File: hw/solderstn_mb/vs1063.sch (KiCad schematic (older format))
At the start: 0 parts

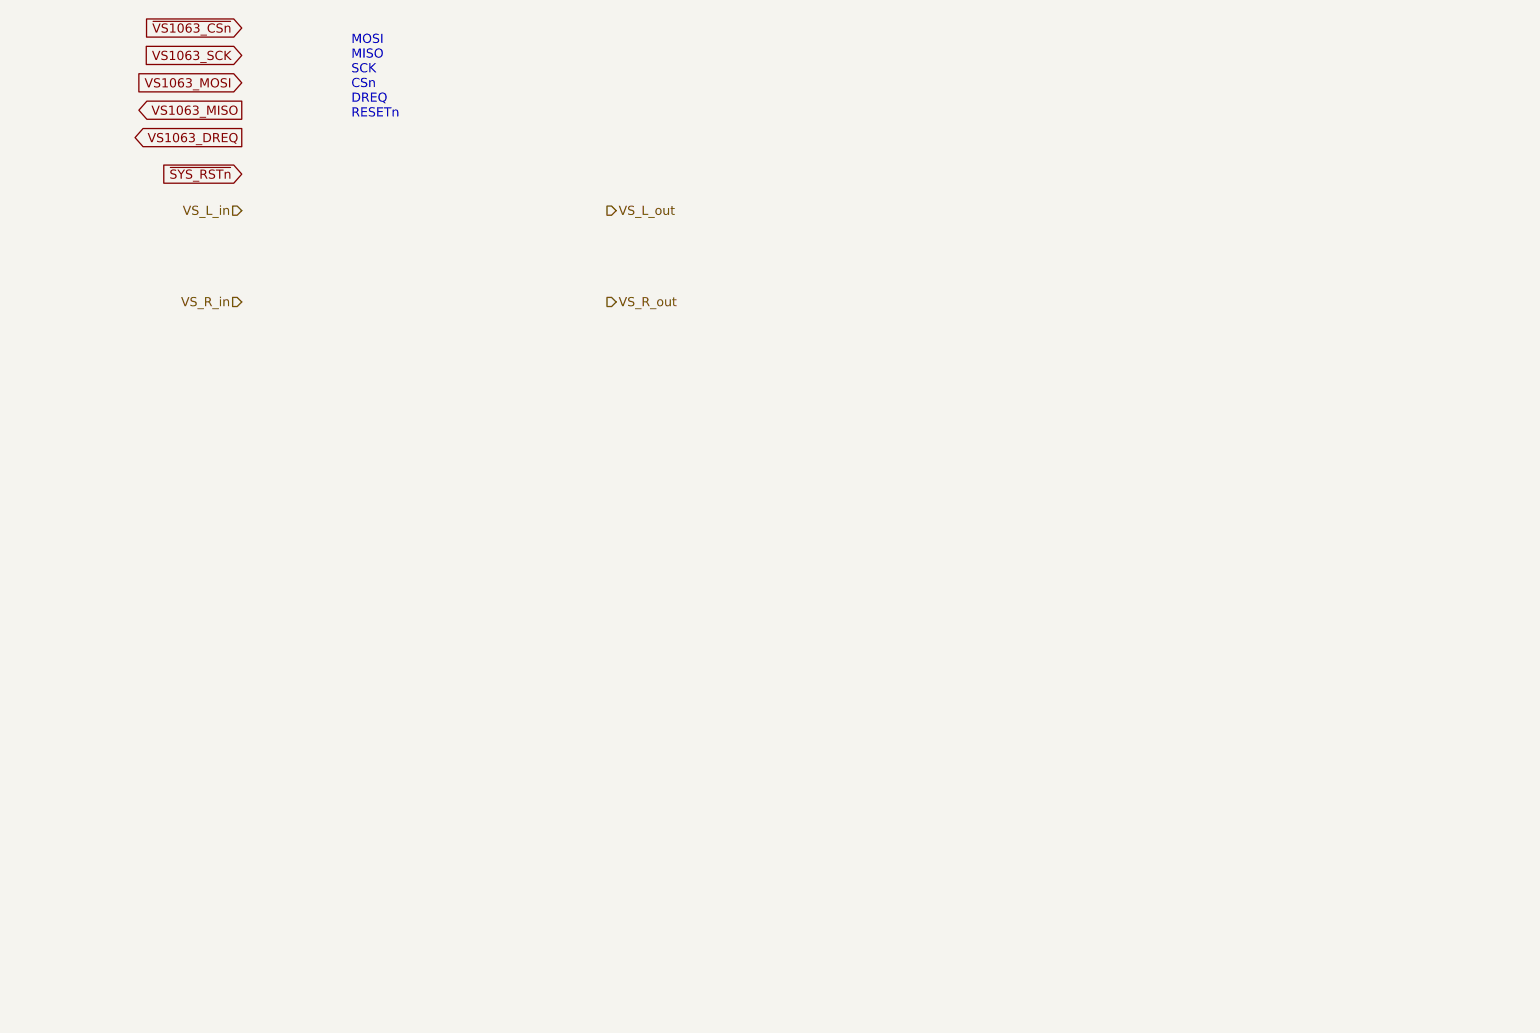
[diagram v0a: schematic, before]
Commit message: MB - Sch design: VS1063 in new audio path; Added: some new ESD, some fixups; Changes: some footprints, fixes
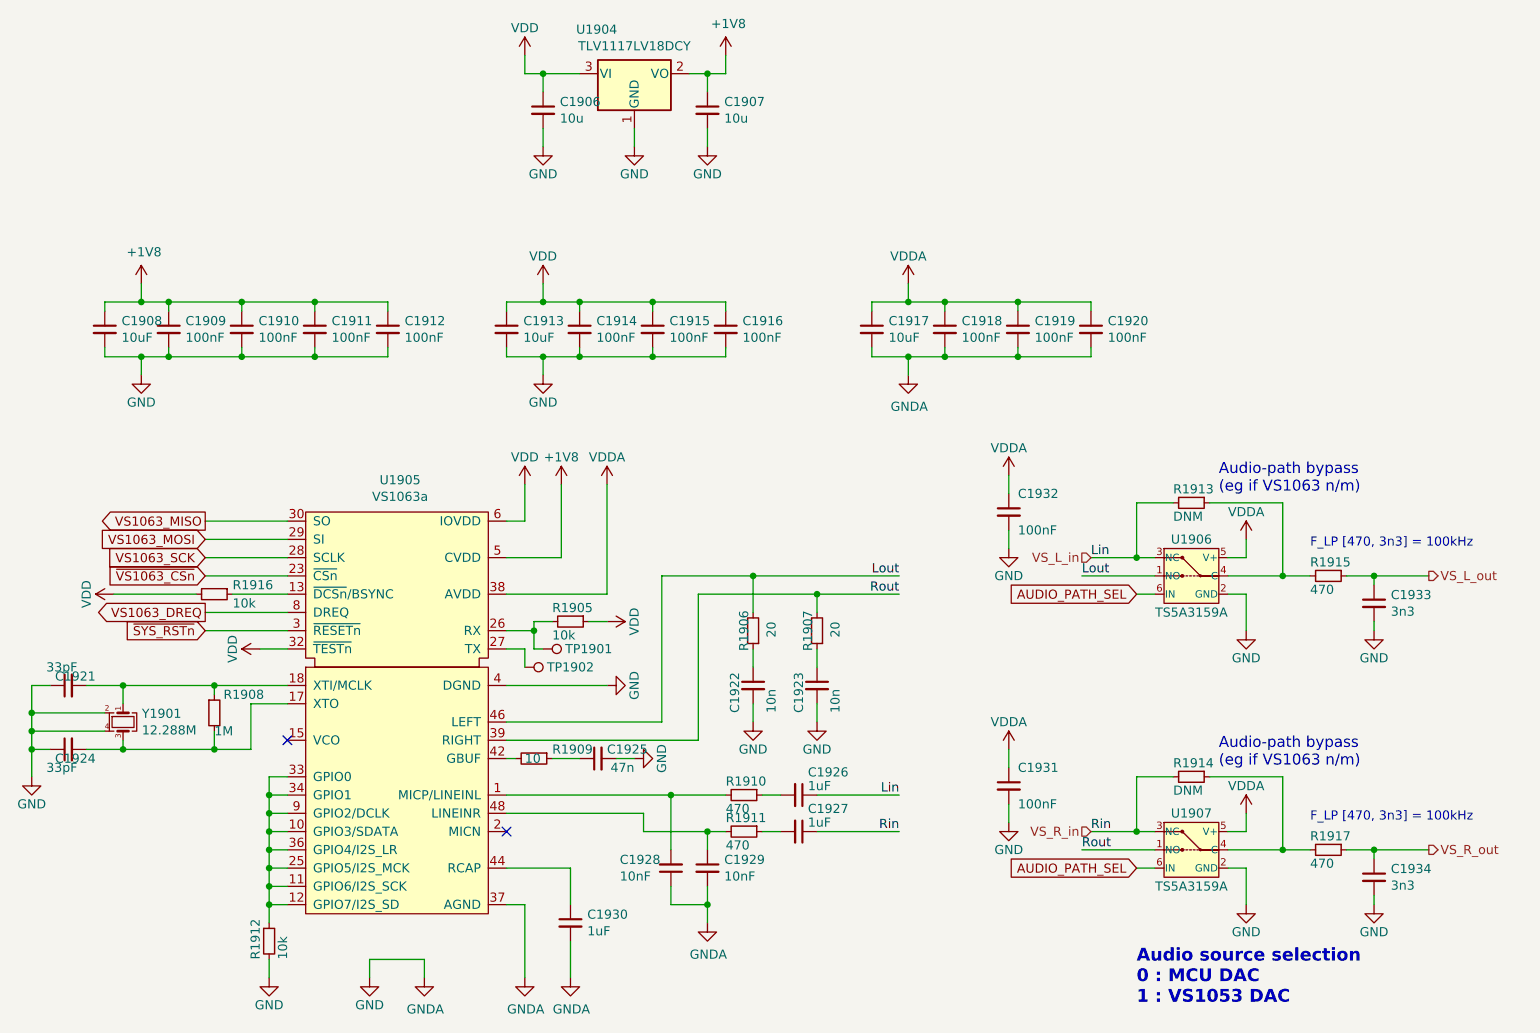
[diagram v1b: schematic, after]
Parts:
- added C1906, C1907: 10u, Capacitor_SMD:C_0603_1608Metric, symbol Device:C_Small
- added C1908, C1913, C1917: 10uF, Capacitor_SMD:C_0603_1608Metric, symbol Device:C_Small
- added C1909, C1910, C1911, C1912, C1914, C1915, C1916, C1918, C1919, C1920, C1931, C1932: 100nF, Capacitor_SMD:C_0402_1005Metric, symbol Device:C_Small
- added C1921, C1924: 33pF, Capacitor_SMD:C_0402_1005Metric, symbol Device:C_Small
- added C1922, C1923: 10n, Capacitor_SMD:C_0402_1005Metric, symbol Device:C_Small
- added C1925: 47n, Capacitor_SMD:C_0402_1005Metric, symbol Device:C_Small
- added C1926, C1927, C1930: 1uF, Capacitor_SMD:C_0603_1608Metric, symbol Device:C_Small
- added C1928, C1929: 10nF, Capacitor_SMD:C_0402_1005Metric, symbol Device:C_Small
- added C1933, C1934: 3n3, Capacitor_SMD:C_0402_1005Metric, symbol Device:C_Small
- added R1905, R1912, R1916: 10k, Resistor_SMD:R_0402_1005Metric, symbol customlib_mj:R_Small
- added R1906, R1907: 20, Resistor_SMD:R_0402_1005Metric, symbol customlib_mj:R_Small
- added R1908: 1M, Resistor_SMD:R_0402_1005Metric, symbol customlib_mj:R_Small
- added R1909: 10, Resistor_SMD:R_0402_1005Metric, symbol customlib_mj:R_Small
- added R1910, R1911, R1915, R1917: 470, Resistor_SMD:R_0402_1005Metric, symbol customlib_mj:R_Small
- added R1913, R1914: DNM, Resistor_SMD:R_0603_1608Metric, symbol customlib_mj:R_Small
- added TP1901, TP1902: TP, customlib_mj_fp:TP_SMD_1.2c, symbol customlib_mj:TP
- added U1904: TLV1117LV18DCY, Package_TO_SOT_SMD:SOT-223-3_TabPin2, symbol customlib_mj:TLV1117LV30DCY
- added U1905: VS1063a, Package_QFP:LQFP-48_7x7mm_P0.5mm, symbol customlib_mj:VS1063a
- added U1906, U1907: TS5A3159A, Package_TO_SOT_SMD:SOT-23-6, symbol customlib_mj:TS5A3159A
- added Y1901: 12.288M, Crystal:Crystal_SMD_SeikoEpson_TSX3225-4Pin_3.2x2.5mm_HandSoldering, symbol customlib_mj:Crystal_ECS­122.8­18­33­JGN­TR
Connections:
- net VS1063_DREQ: now also U1905.8 (DREQ)
- net VS1063_MISO: now also U1905.30 (SO)
- net VS1063_MOSI: now also U1905.29 (SI)
- net VS1063_SCK: now also U1905.28 (SCLK)
- net VS_L_in: now also C1926.1, R1913.2, U1906.3 (NC)
- net VS_L_out: now also C1933.1, R1915.1
- net VS_R_in: now also C1927.1, R1914.2, U1907.3 (NC)
- net VS_R_out: now also C1934.1, R1917.1
- net ~SYS_RSTn~: now also U1905.3 (~RESETn~)
- net ~VS1063_CSn~: now also U1905.23 (~CSn~)
- new net: C1928.2, R1910.2, U1905.1 (MICP/LINEINL)
- new net: R1912.1, U1905.10 (GPIO3/SDATA), U1905.11 (GPIO6/I2S_SCK), U1905.12 (GPIO7/I2S_SD), U1905.25 (GPIO5/I2S_MCK), U1905.33 (GPIO0), U1905.34 (GPIO1), U1905.36 (GPIO4/I2S_LR), U1905.9 (GPIO2/DCLK)
- new net: R1916.1, U1905.13 (~DCSn~/BSYNC)
- new net: C1924.2, R1908.2, U1905.17 (XTO), Y1901.3
- new net: C1921.2, R1908.1, U1905.18 (XTI/MCLK), Y1901.1
- new net: R1905.2, TP1901.1, U1905.26 (RX)
- new net: TP1902.1, U1905.27 (TX)
- new net: R1909.2, U1905.42 (GBUF)
- new net: C1930.1, U1905.44 (RCAP)
- new net: C1929.1, R1911.2, U1905.48 (LINEINR)
- new net: C1926.2, R1910.1
- new net: C1927.2, R1911.1
- new net: C1925.1, R1909.1
- new net: C1923.1, R1907.1
- new net: C1922.1, R1906.1
- new net: R1913.1, R1915.2, U1906.4 (C)
- new net: R1914.1, R1917.2, U1907.4 (C)
- new net +1V8: C1907.1, C1908.1, C1909.1, C1910.1, C1911.1, C1912.1, U1904.2 (VO), U1905.24 (CVDD), U1905.31 (CVDD), U1905.5 (CVDD), U1905.7 (CVDD)
- new net AGND: C1906.2, C1907.2, C1908.2, C1909.2, C1910.2, C1911.2, C1912.2, C1913.2, C1914.2, C1915.2, C1916.2, C1917.2, C1918.2, C1919.2, C1920.2, C1921.1, C1922.2, C1923.2, C1924.1, C1925.2, C1928.1, C1929.2, C1930.2, C1931.2, C1932.2, C1933.2, C1934.2, R1912.2, U1904.1 (GND), U1905.16 (DGND), U1905.20 (DGND), U1905.21 (DGND), U1905.22 (DGND), U1905.35 (DGND), U1905.37 (AGND), U1905.4 (DGND), U1905.40 (AGND), U1905.41 (AGND), U1905.47 (AGND), U1906.2 (GND), U1907.2 (GND), Y1901.2, Y1901.4
- new net AUDIO_PATH_SEL: U1906.6 (IN), U1907.6 (IN)
- new net AVDD: C1917.1, C1918.1, C1919.1, C1920.1, C1931.1, C1932.1, U1905.38 (AVDD), U1905.43 (AVDD), U1905.45 (AVDD), U1906.5 (V+), U1907.5 (V+)
- new net IOVDD: C1906.1, C1913.1, C1914.1, C1915.1, C1916.1, R1905.1, R1916.2, U1904.3 (VI), U1905.14 (IOVDD), U1905.19 (IOVDD), U1905.32 (~TESTn~), U1905.6 (IOVDD)
- new net Lout: R1906.2, U1905.46 (LEFT), U1906.1 (NO)
- new net Rout: R1907.2, U1905.39 (RIGHT), U1907.1 (NO)
- no-connect marks 0 -> 2
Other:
- note added: "Audio source selection\n0 : MCU DAC\n1 : VS1053 DAC"
- note added: "Audio-path bypass\n(eg if VS1063 n/m)"
- note added: "F_LP [470, 3n3] = 100kHz"
- note removed: "MOSI\nMISO\nSCK\nCSn\nDREQ\nRESETn"

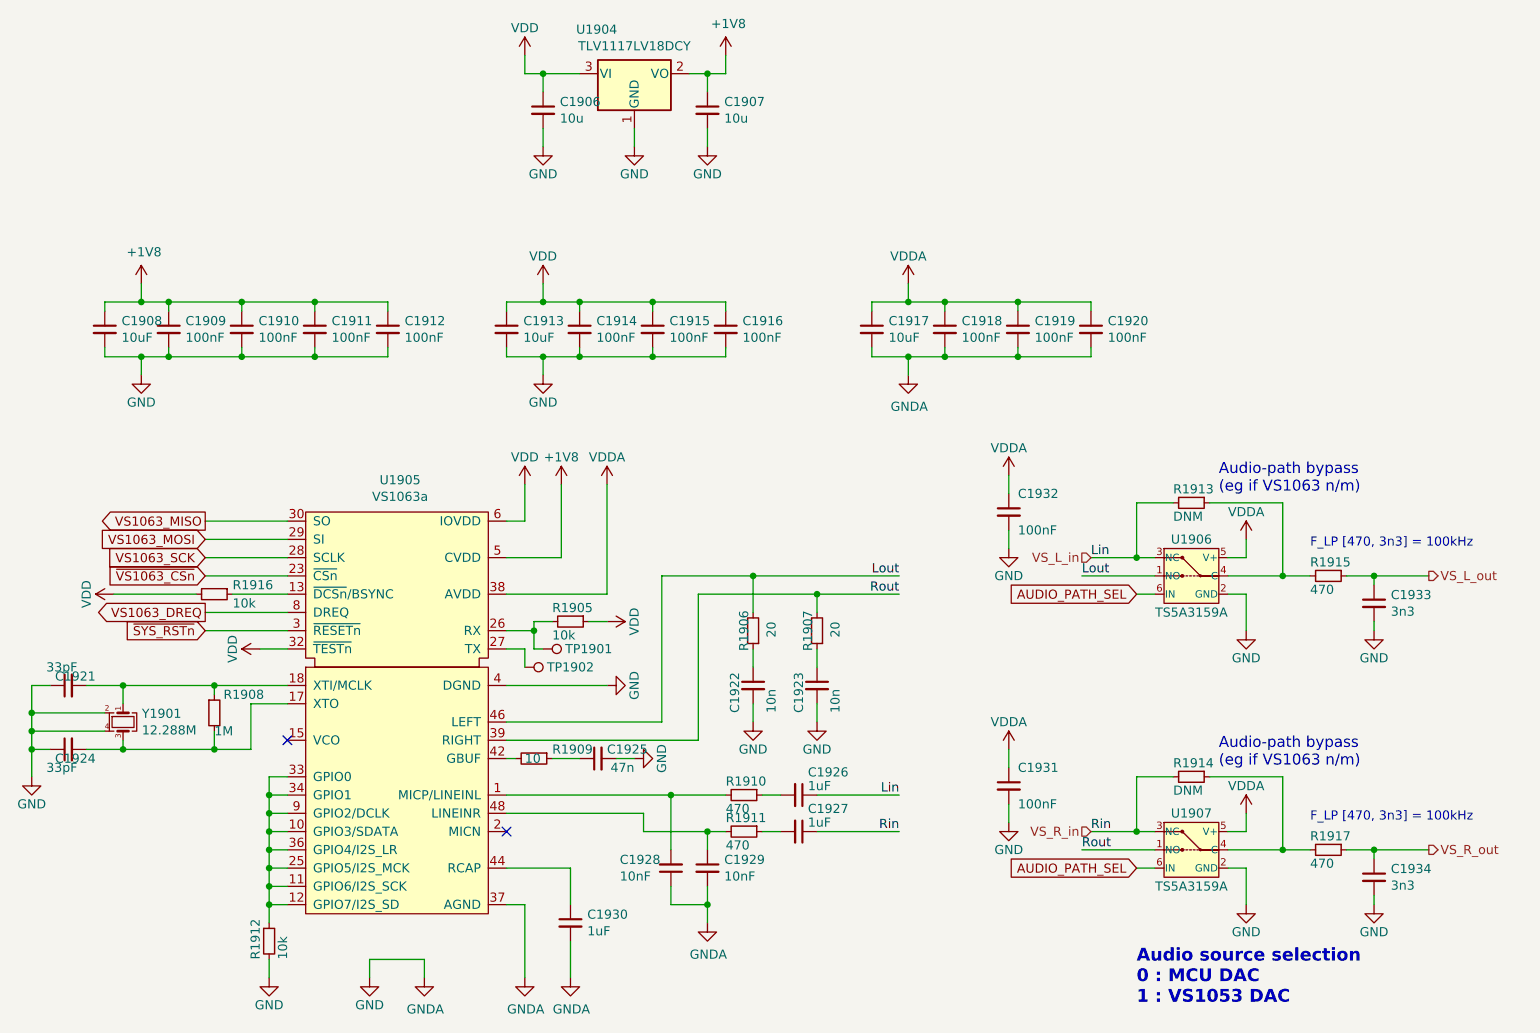
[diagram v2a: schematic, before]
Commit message: Reannotate entire schematic; add temp.extra SMA-conn to eval alternative FMI placement
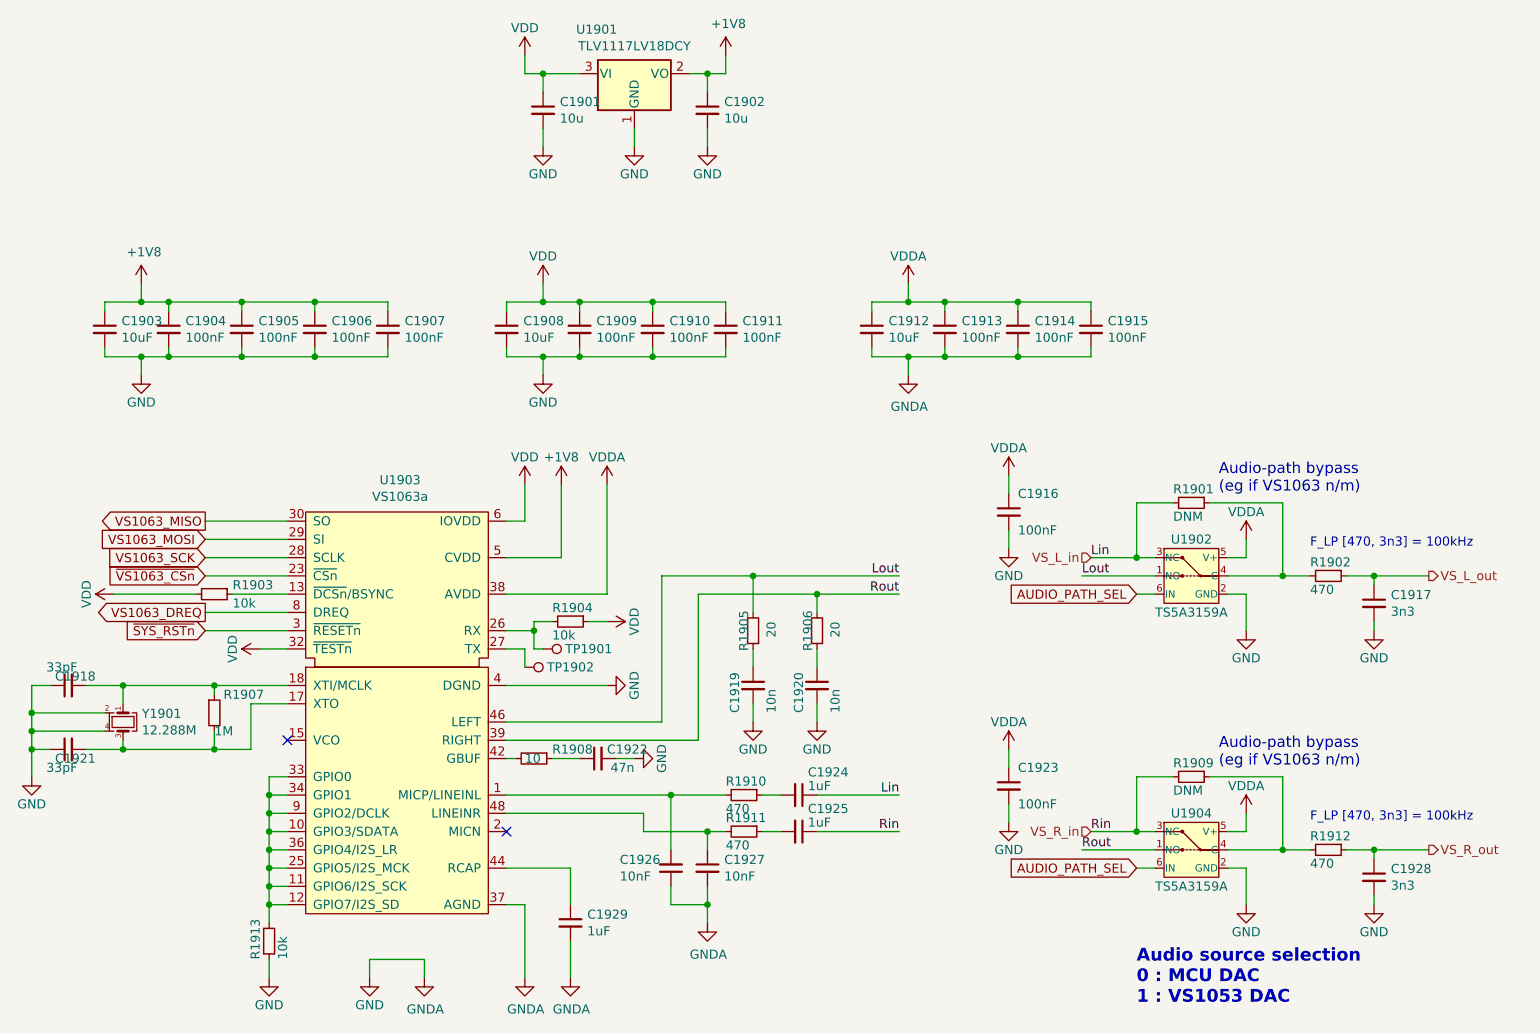
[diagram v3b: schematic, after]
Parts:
- renumbered C1906 to C1901, C1907 to C1902, C1908 to C1903, C1909 to C1904, C1910 to C1905, C1911 to C1906, C1912 to C1907, C1913 to C1908, C1914 to C1909, C1915 to C1910, C1916 to C1911, C1917 to C1912, C1918 to C1913, C1919 to C1914, C1920 to C1915, C1932 to C1916, C1933 to C1917, C1921 to C1918, C1922 to C1919, C1923 to C1920, C1924 to C1921, C1925 to C1922, C1931 to C1923, C1926 to C1924, C1927 to C1925, C1928 to C1926, C1929 to C1927, C1934 to C1928, C1930 to C1929, R1913 to R1901, R1915 to R1902, R1916 to R1903, R1905 to R1904, R1906 to R1905, R1907 to R1906, R1908 to R1907, R1909 to R1908, R1914 to R1909, R1917 to R1912, R1912 to R1913, U1904 to U1901, U1906 to U1902, U1905 to U1903, U1907 to U1904
